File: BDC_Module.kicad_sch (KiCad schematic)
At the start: 21 parts, among them J1 Conn_01x10_Pin, J2 Conn_01x10_Pin, J3 Conn_01x10_Pin, U1 TPS54531DDA

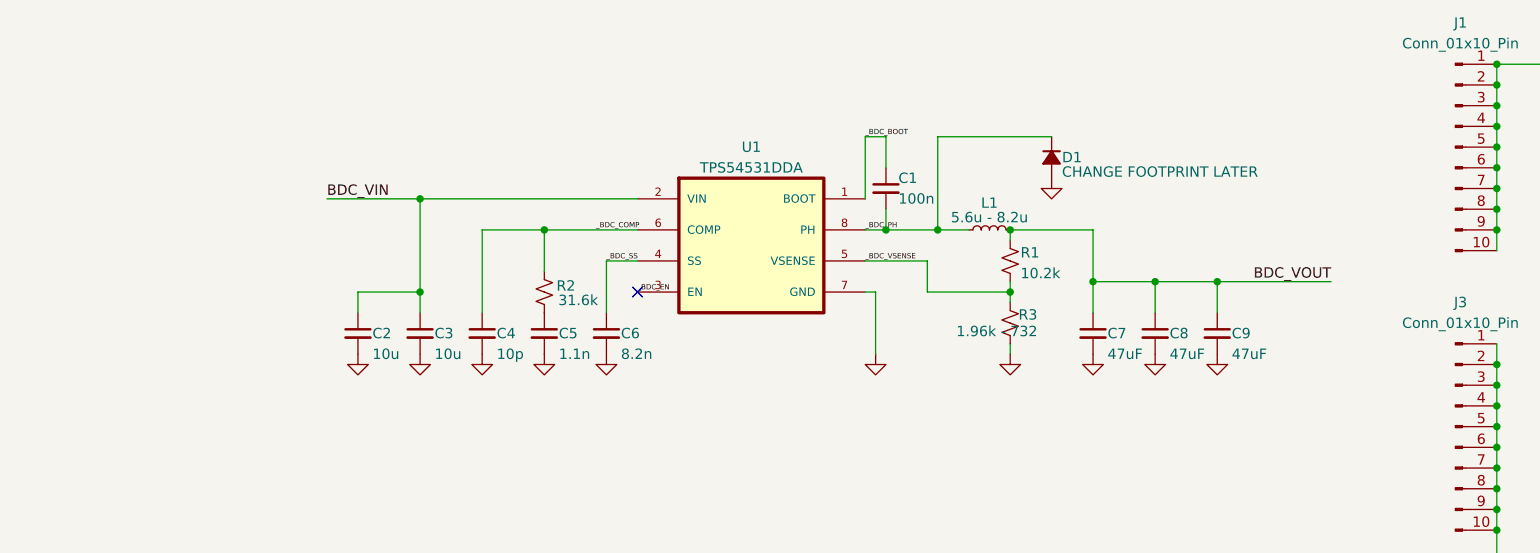
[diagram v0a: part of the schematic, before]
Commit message: add Fuse, LEDs
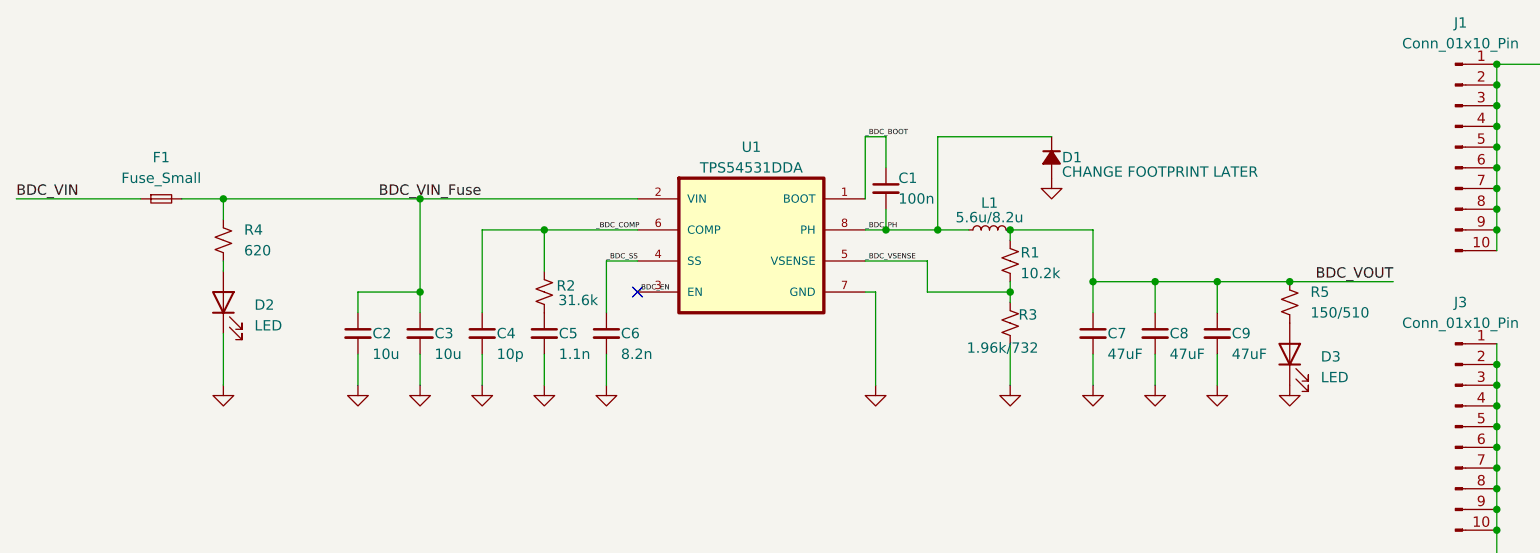
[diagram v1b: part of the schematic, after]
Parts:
- added D2, D3: LED, LED_SMD:LED_1206_3216Metric, symbol Device:LED
- added F1: Fuse_Small, Fuse:Fuse_1206_3216Metric, symbol Device:Fuse_Small
- added R4: 620, Resistor_SMD:R_0603_1608Metric, symbol Device:R_Small_US
- added R5: 150/510, Resistor_SMD:R_0603_1608Metric, symbol Device:R_Small_US
- L1: value 5.6u - 8.2u -> 5.6u/8.2u
- R3: value 1.96k - 732 -> 1.96k/732
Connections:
- net BDC_VIN: now also F1.1; no longer C2.1, C3.1, U1.2 (VIN)
- net BDC_VOUT: now also R5.1
- net GND: now also D2.1 (K), D3.1 (K)
- new net: D2.2 (A), R4.2
- new net: D3.2 (A), R5.2
- new net BDC_VIN_Fuse: C2.1, C3.1, F1.2, R4.1, U1.2 (VIN)

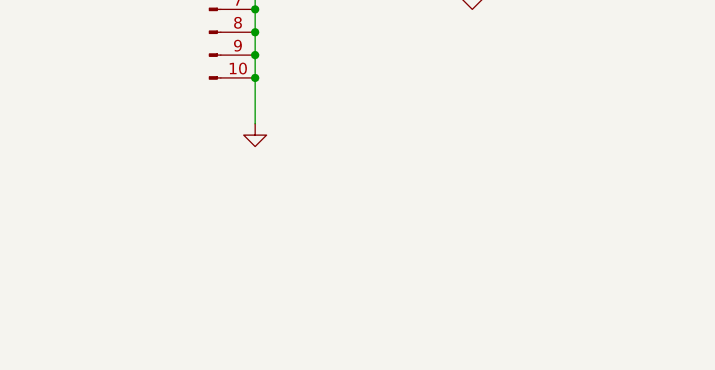
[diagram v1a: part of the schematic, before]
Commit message: Add XT30 connectors
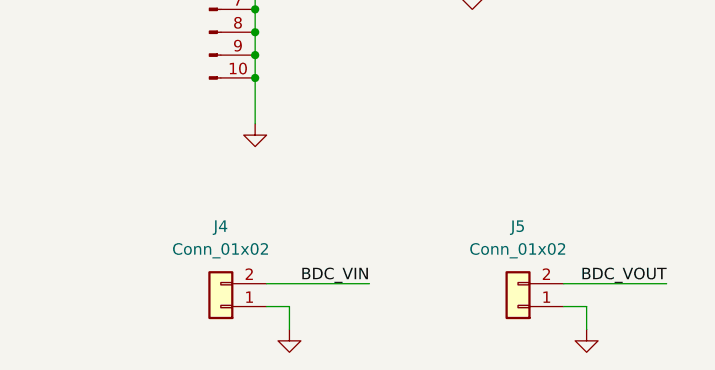
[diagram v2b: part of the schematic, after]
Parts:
- added J4, J5: Conn_01x02, Connector_AMASS:AMASS_XT30U-F_1x02_P5.0mm_Vertical, symbol Connector_Generic:Conn_01x02
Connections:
- net BDC_VIN: now also J4.2 (Pin_2)
- net BDC_VOUT: now also J5.2 (Pin_2)
- net GND: now also J4.1 (Pin_1), J5.1 (Pin_1)

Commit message: update mounting
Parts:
- removed J1, J2, J3: Conn_01x10_Pin, Connector_PinHeader_2.54mm:PinHeader_1x10_P2.54mm_Vertical, symbol Connector:Conn_01x10_Pin
- added J1, J2: Conn_01x02, Connector_AMASS:AMASS_XT30U-F_1x02_P5.0mm_Vertical, symbol Connector_Generic:Conn_01x02
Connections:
- net BDC_VIN: no longer TP1.1
- net BDC_VIN_Fuse: now also TP1.1
- net GND: now also J1.1 (Pin_1), J1.2 (Pin_2), J2.1 (Pin_1), J2.2 (Pin_2)
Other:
- moved on the sheet: J4, J5, TP1, TP2, TP3

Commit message: Finalize schematic & layout
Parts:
- removed D2, D3: LED, LED_SMD:LED_1206_3216Metric, symbol Device:LED
- removed F1: Fuse_Small, Fuse:Fuse_1206_3216Metric, symbol Device:Fuse_Small
- removed J1, J2, J4, J5: Conn_01x02, Connector_AMASS:AMASS_XT30U-F_1x02_P5.0mm_Vertical, symbol Connector_Generic:Conn_01x02
- removed R4: 620, Resistor_SMD:R_0603_1608Metric, symbol Device:R_Small_US
- removed R5: 150/510, Resistor_SMD:R_0603_1608Metric, symbol Device:R_Small_US
- added C10: 10u, Capacitor_SMD:C_0805_2012Metric, symbol Device:C_Small
- added H1, H2, H3, H4: M2, MountingHole:MountingHole_2.2mm_M2, symbol Mechanical:MountingHole
- added J1, J2: XT-30, Connector_AMASS:AMASS_XT60-F_1x02_P7.20mm_Vertical, symbol Connector:Conn_01x02_Socket
- D1: footprint Diode_SMD:D_0805_2012Metric -> Diode_SMD:D_SMC
- L1: value 5.6u/8.2u -> 5.6u; footprint Inductor_SMD:L_APV_ANR4018 -> Inductor_SMD:L_Vishay_IHLP-2525
- R3: value 1.96k/732 -> 1.96k
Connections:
- net BDC_VIN_Fuse is gone; now on net BDC_VIN: C2.1, C3.1, TP1.1, U1.2 (VIN)
- net BDC_VIN: now also C10.1, J1.2 (Pin_2)
- net BDC_VOUT: now also J2.2 (Pin_2)
- net GND: now also C10.2, J1.1 (Pin_1), J2.1 (Pin_1)
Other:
- moved on the sheet: TP2, TP3
